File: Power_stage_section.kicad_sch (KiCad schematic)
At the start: 31 parts, among them IC1 LM66200DRLR, Q1 BSC082N10LSG, Q2 BSC082N10LSG, U2 IRS2186, U3 TLV70012_SOT23-5

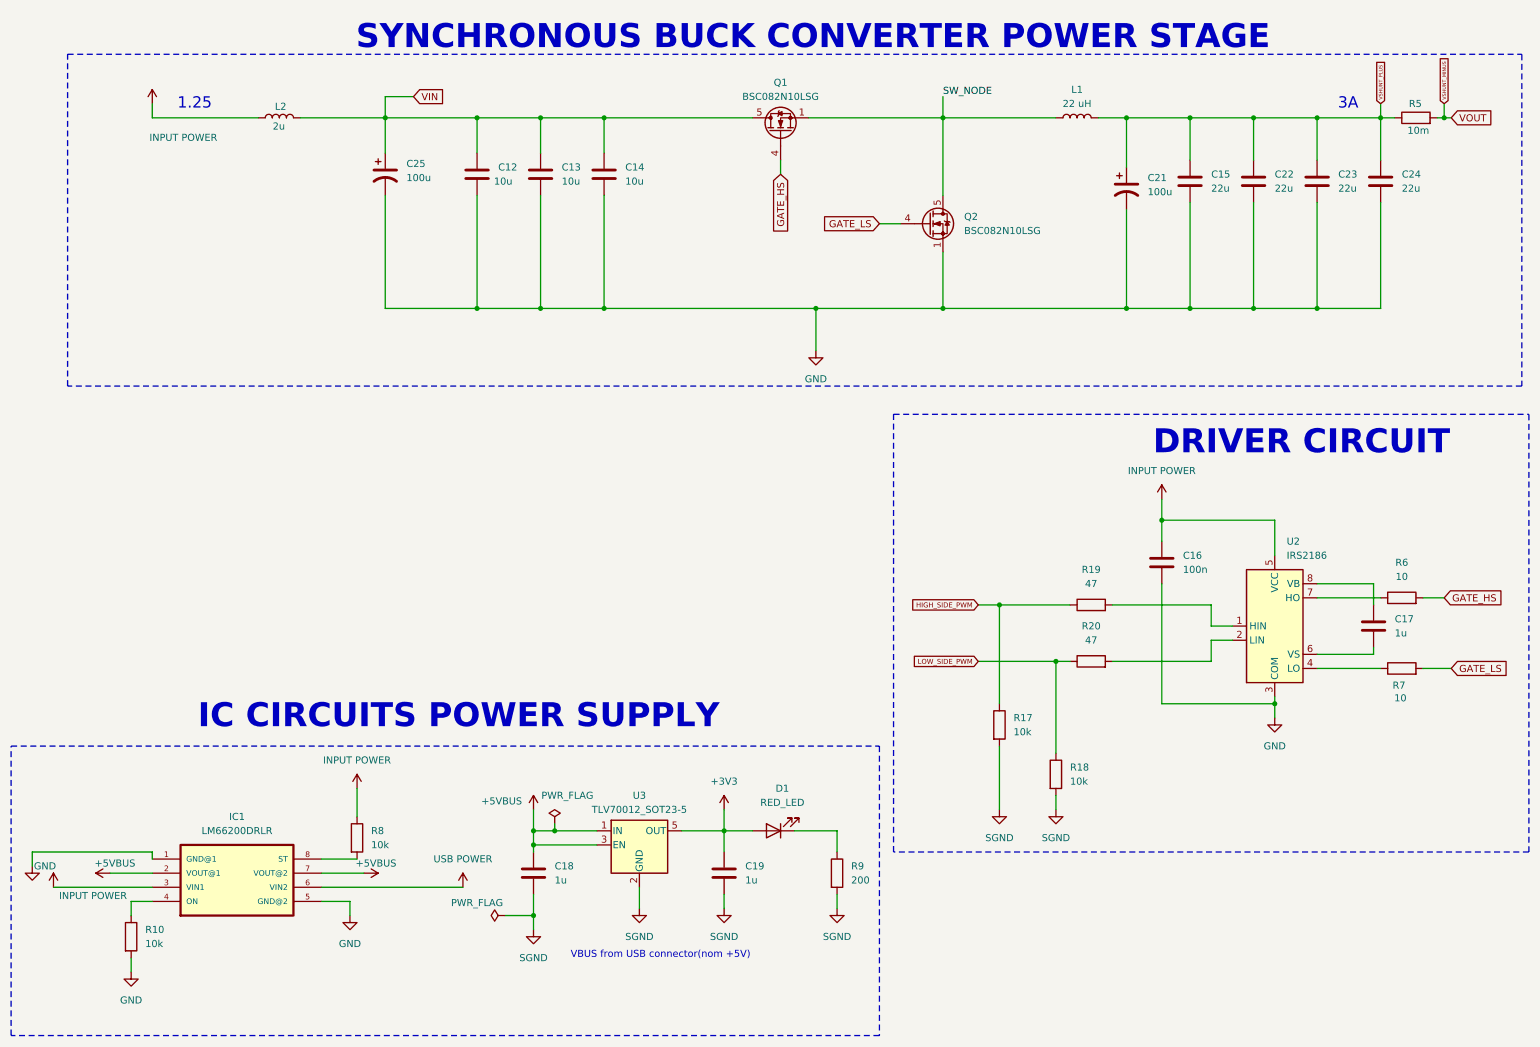
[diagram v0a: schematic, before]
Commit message: Power loop routed
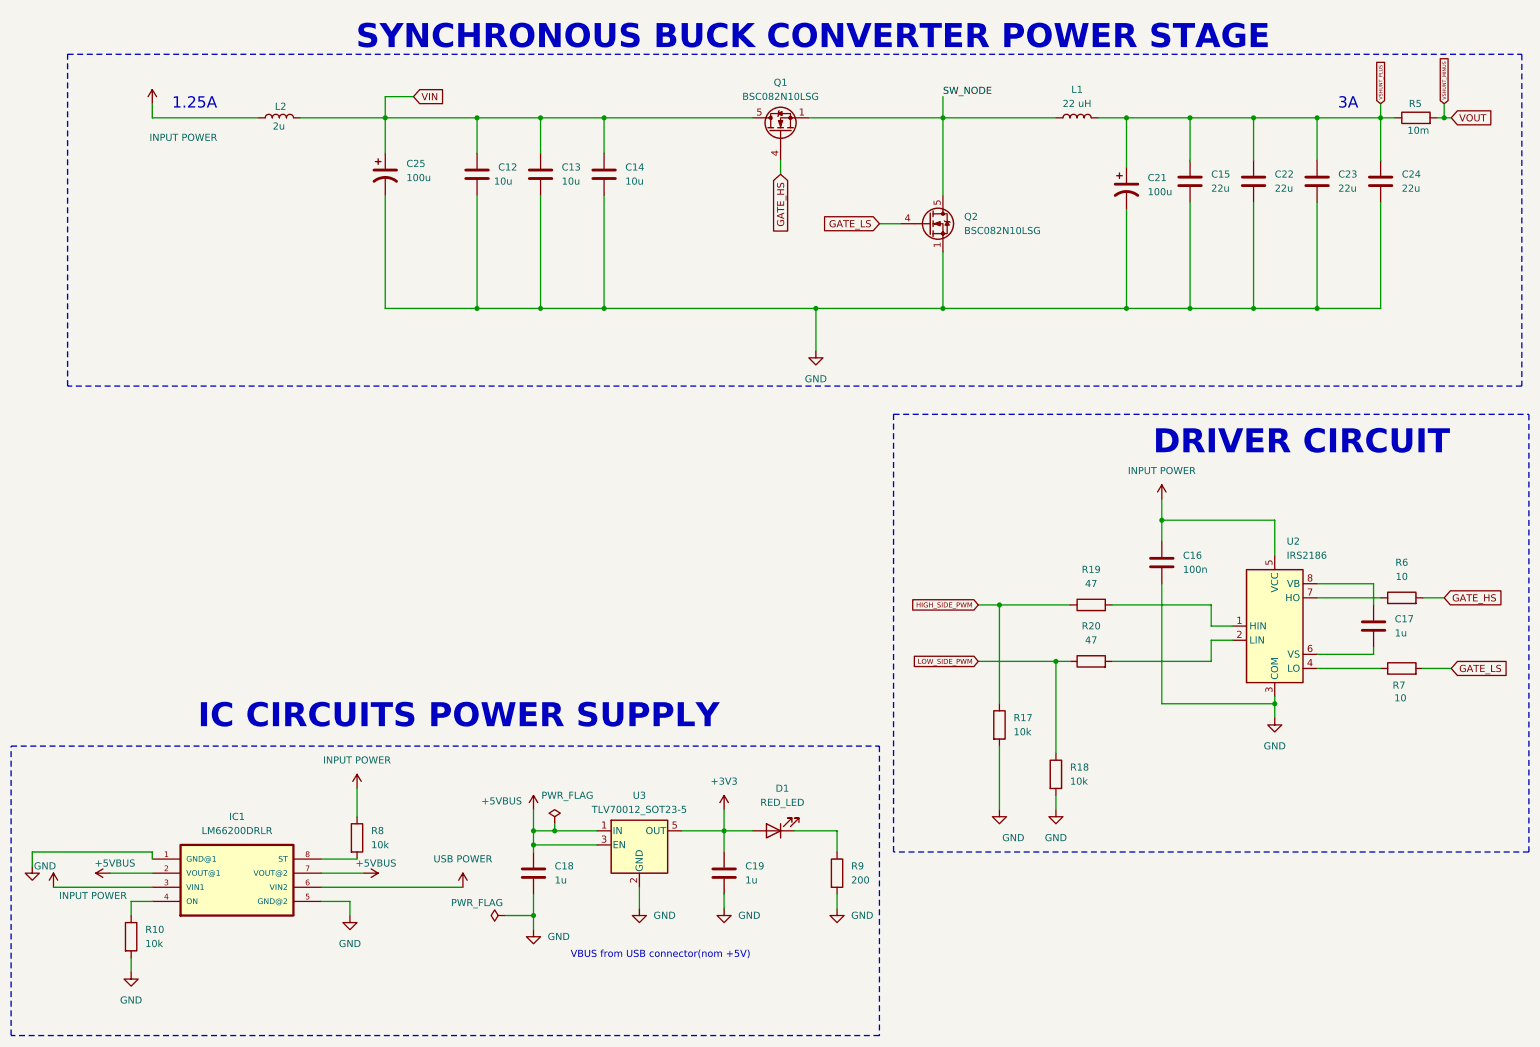
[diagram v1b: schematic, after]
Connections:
- net SGND is gone; now on net GND: C18.2, C19.2, R17.2, R18.2, R9.2, U3.2 (GND)
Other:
- note added: "1.25A"
- note removed: "1.25"
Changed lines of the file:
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@@
 		)
 	)
-	(text "1.25\n"
+	(text "1.25A\n"
 		(exclude_from_sim no)
 		(at 45.72 27.94 0)
@@
 		(on_board yes)
 		(dnp no)
-		(fields_autoplaced yes)
 		(property "Reference" "#PWR066"
 			(at 190.5 161.29 0)
@@
 			)
 		)
-		(property "Value" "SGND"
-			(at 190.5 160.02 0)
+		(property "Value" "GND"
+			(at 191.008 160.02 0)
 			(effects
 				(font
 					(size 1.27 1.27)
 				)
+				(justify left)
 			)
 		)
@@
 			)
 		)
-		(property "Value" "SGND"
-			(at 140.97 177.8 0)
+		(property "Value" "GND"
+			(at 143.51 173.9899 0)
 			(effects
 				(font
 					(size 1.27 1.27)
 				)
+				(justify left)
 			)
 		)
@@
 			)
 		)
-		(property "Value" "SGND"
-			(at 106.68 181.61 0)
+		(property "Value" "GND"
+			(at 109.22 177.7999 0)
 			(effects
 				(font
 					(size 1.27 1.27)
 				)
+				(justify left)
 			)
 		)
@@
 			)
 		)
-		(property "Value" "SGND"
-			(at 125.73 177.8 0)
+		(property "Value" "GND"
+			(at 128.27 173.9899 0)
 			(effects
 				(font
 					(size 1.27 1.27)
 				)
+				(justify left)
 			)
 		)
@@
 			)
 		)
-		(property "Value" "SGND"
+		(property "Value" "GND"
 			(at 200.66 160.02 0)
 			(effects
@@
 			)
 		)
-		(property "Value" "SGND"
-			(at 161.29 177.8 0)
+		(property "Value" "GND"
+			(at 163.83 173.9899 0)
 			(effects
 				(font
 					(size 1.27 1.27)
 				)
+				(justify left)
 			)
 		)
